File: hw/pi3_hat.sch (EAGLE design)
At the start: 117 parts, among them J1 XT30P, J2 XT30P, U1 AP64351SO8EP, U10 CAT24C32SOIC8, U11 STM32G474CEU6, U12 TCAN334GSOT23, U13 TCAN334GSOT23, U14 SPW2430HR5H-B, U2 DMMT5401, U3 DMG2305UX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

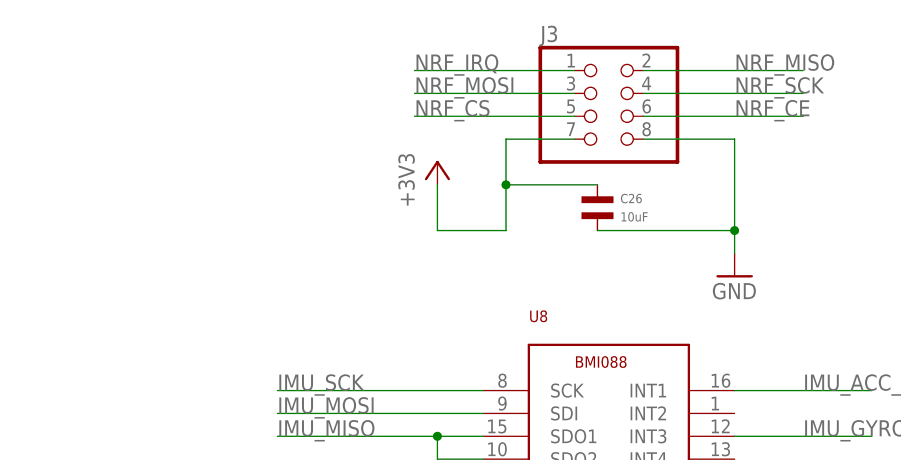
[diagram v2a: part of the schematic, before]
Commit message: Flip NRF around, add an LC filter and a ground plane
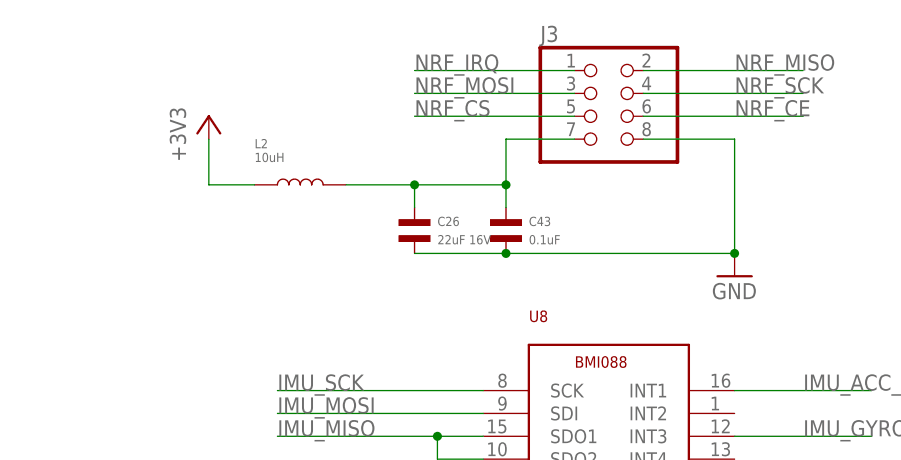
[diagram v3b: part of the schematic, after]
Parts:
- added C43: 0.1uF, mfpassives:CAPACITOR_NP_0402
- added L2: 10uH, mfpassives:INDUCTOR_1210
- C26: value 10uF -> 22uF 16V; device mfpassives:CAPACITOR_NP_1206 -> mfpassives:CAPACITOR_NP_1210; HOUSEPART YES -> (none); MF (none) -> SAMSUNG; MPN MF-CAP-1206-10uF -> CL32A226KOJNNNE
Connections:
- new net N$56: C26.P$1, C43.P$1, J3.7, L2.P$2
- net +3V3: now also L2.P$1; no longer C26.P$1, J3.7
- net GND: now also C43.P$2
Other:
- moved on the sheet: C26
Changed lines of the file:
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@@
 <part name="GND39" library="supply1" deviceset="GND" device=""/>
 <part name="+3V22" library="supply1" deviceset="+3V3" device=""/>
-<part name="C26" library="mfpassives" deviceset="CAPACITOR_NP" device="_1206" value="10uF">
-<attribute name="HOUSEPART" value="YES"/>
-<attribute name="MPN" value="MF-CAP-1206-10uF"/>
-</part>
 <part name="+3V25" library="supply1" deviceset="+3V3" device=""/>
 <part name="U10" library="pi3_hat" deviceset="CAT24C32" device="SOIC8">
@@
 <attribute name="MPN" value="MF-CAP-1206-10uF"/>
 </part>
+<part name="L2" library="mfpassives" deviceset="INDUCTOR" device="_1210" value="10uH">
+<attribute name="MPN" value="MF-IND-1210-10uH"/>
+</part>
+<part name="C43" library="mfpassives" deviceset="CAPACITOR_NP" device="_0402" value="0.1uF">
+<attribute name="HOUSEPART" value="YES"/>
+<attribute name="MPN" value="MF-CAP-0402-0.1uF"/>
+</part>
+<part name="C26" library="mfpassives" deviceset="CAPACITOR_NP" device="_1210" value="22uF 16V">
+<attribute name="MF" value="SAMSUNG"/>
+<attribute name="MPN" value="CL32A226KOJNNNE"/>
+</part>
 </parts>
 <sheets>
@@
 <attribute name="VALUE" x="812.8" y="307.34" size="1.778" layer="96"/>
 </instance>
-<instance part="+3V22" gate="G$1" x="782.32" y="322.58" smashed="yes">
-<attribute name="VALUE" x="779.78" y="317.5" size="1.778" layer="96" rot="R90"/>
-</instance>
-<instance part="C26" gate="G$1" x="800.1" y="317.5" smashed="yes">
-<attribute name="NAME" x="802.64" y="319.024" size="1.016" layer="95" font="vector" align="top-left"/>
-<attribute name="VALUE" x="802.64" y="315.976" size="1.016" layer="96" font="vector"/>
+<instance part="+3V22" gate="G$1" x="756.92" y="327.66" smashed="yes">
+<attribute name="VALUE" x="754.38" y="322.58" size="1.778" layer="96" rot="R90"/>
 </instance>
 <instance part="+3V25" gate="G$1" x="355.6" y="261.62" smashed="yes">
@@
 <attribute name="VALUE" x="801.624" y="60.96" size="1.016" layer="96" font="vector" rot="R90"/>
 </instance>
+<instance part="L2" gate="G$1" x="767.08" y="320.04" smashed="yes">
+<attribute name="NAME" x="762" y="325.12" size="1.016" layer="95" font="vector" align="top-left"/>
+<attribute name="VALUE" x="762" y="322.58" size="1.016" layer="96" font="vector"/>
+</instance>
+<instance part="C43" gate="G$1" x="789.94" y="314.96" smashed="yes">
+<attribute name="NAME" x="792.48" y="316.484" size="1.016" layer="95" font="vector" align="top-left"/>
+<attribute name="VALUE" x="792.48" y="313.436" size="1.016" layer="96" font="vector"/>
+</instance>
+<instance part="C26" gate="G$1" x="779.78" y="314.96" smashed="yes">
+<attribute name="MF" x="779.78" y="314.96" size="1.778" layer="96" display="off"/>
+<attribute name="NAME" x="782.32" y="316.484" size="1.016" layer="95" font="vector" align="top-left"/>
+<attribute name="VALUE" x="782.32" y="313.436" size="1.016" layer="96" font="vector"/>
+</instance>
 </instances>
 <busses>
@@
 <pinref part="GND39" gate="1" pin="GND"/>
 <wire x1="805.18" y1="325.12" x2="815.34" y2="325.12" width="0.1524" layer="91"/>
-<wire x1="815.34" y1="325.12" x2="815.34" y2="314.96" width="0.1524" layer="91"/>
+<wire x1="815.34" y1="325.12" x2="815.34" y2="312.42" width="0.1524" layer="91"/>
+<wire x1="789.94" y1="312.42" x2="815.34" y2="312.42" width="0.1524" layer="91"/>
+<junction x="815.34" y="312.42"/>
+<pinref part="C43" gate="G$1" pin="P$2"/>
 <pinref part="C26" gate="G$1" pin="P$2"/>
-<wire x1="815.34" y1="314.96" x2="815.34" y2="312.42" width="0.1524" layer="91"/>
-<wire x1="800.1" y1="314.96" x2="815.34" y2="314.96" width="0.1524" layer="91"/>
-<junction x="815.34" y="314.96"/>
+<wire x1="779.78" y1="312.42" x2="789.94" y2="312.42" width="0.1524" layer="91"/>
+<junction x="789.94" y="312.42"/>
 </segment>
 <segment>
@@
 </segment>
 <segment>
-<pinref part="+3V22" gate="G$1" pin="+3V3"/>
-<wire x1="782.32" y1="320.04" x2="782.32" y2="314.96" width="0.1524" layer="91"/>
-<wire x1="782.32" y1="314.96" x2="789.94" y2="314.96" width="0.1524" layer="91"/>
-<wire x1="789.94" y1="314.96" x2="789.94" y2="320.04" width="0.1524" layer="91"/>
-<pinref part="J3" gate="A" pin="7"/>
-<wire x1="789.94" y1="320.04" x2="789.94" y2="325.12" width="0.1524" layer="91"/>
-<wire x1="789.94" y1="325.12" x2="797.56" y2="325.12" width="0.1524" layer="91"/>
-<pinref part="C26" gate="G$1" pin="P$1"/>
-<wire x1="789.94" y1="320.04" x2="800.1" y2="320.04" width="0.1524" layer="91"/>
-<junction x="789.94" y="320.04"/>
-</segment>
-<segment>
 <pinref part="U4" gate="G$1" pin="VBAT"/>
 <pinref part="+3V25" gate="G$1" pin="+3V3"/>
@@
 <wire x1="802.64" y1="63.5" x2="792.48" y2="63.5" width="0.1524" layer="91"/>
 </segment>
+<segment>
+<pinref part="+3V22" gate="G$1" pin="+3V3"/>
+<wire x1="756.92" y1="325.12" x2="756.92" y2="320.04" width="0.1524" layer="91"/>
+<pinref part="L2" gate="G$1" pin="P$1"/>
+<wire x1="756.92" y1="320.04" x2="762" y2="320.04" width="0.1524" layer="91"/>
+</segment>
 </net>
 <net name="PI_TX_3V" class="0">
@@
 </segment>
 </net>
+<net name="N$56" class="0">
+<segment>
+<wire x1="772.16" y1="320.04" x2="779.78" y2="320.04" width="0.1524" layer="91"/>
+<pinref part="J3" gate="A" pin="7"/>
+<wire x1="779.78" y1="320.04" x2="789.94" y2="320.04" width="0.1524" layer="91"/>
+<wire x1="789.94" y1="320.04" x2="789.94" y2="325.12" width="0.1524" layer="91"/>
+<wire x1="789.94" y1="325.12" x2="797.56" y2="325.12" width="0.1524" layer="91"/>
+<wire x1="789.94" y1="320.04" x2="789.94" y2="317.5" width="0.1524" layer="91"/>
+<junction x="789.94" y="320.04"/>
+<pinref part="L2" gate="G$1" pin="P$2"/>
+<pinref part="C43" gate="G$1" pin="P$1"/>
+<pinref part="C26" gate="G$1" pin="P$1"/>
+<wire x1="779.78" y1="317.5" x2="779.78" y2="320.04" width="0.1524" layer="91"/>
+<junction x="779.78" y="320.04"/>
+</segment>
+</net>

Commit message: Update board rev to 4.1, since we haven't made one of those yet
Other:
- note added: "mjbots pi3 hat r4.1 (c) jjp@pobox.com 2020 Licensed under the Apache 2.0 License"
- note removed: "mjbots pi3 hat r4.2 (c) jjp@pobox.com 2020 Licensed under the Apache 2.0 License"
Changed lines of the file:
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@@
 <wire x1="-48.26" y1="170.18" x2="-48.26" y2="347.98" width="0.1524" layer="90"/>
 <text x="-45.72" y="335.28" size="7.62" layer="90" font="vector">INPUT POWER</text>
-<text x="-45.72" y="355.6" size="7.62" layer="90" font="vector">mjbots pi3 hat r4.2
+<text x="-45.72" y="355.6" size="7.62" layer="90" font="vector">mjbots pi3 hat r4.1
 (c) jjp@pobox.com 2020
 Licensed under the Apache 2.0 License</text>

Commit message: Add MPN for LTC2875
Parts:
- U9: MF (none) -> Analog; MPN (none) -> LTC2875IS8#PBF; POPULATE (none) -> 1
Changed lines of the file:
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@@
 <attribute name="POPULATE" value="0"/>
 </part>
-<part name="U9" library="pi3_hat" deviceset="LTC2875" device=""/>
+<part name="U9" library="pi3_hat" deviceset="LTC2875" device="">
+<attribute name="MF" value="Analog"/>
+<attribute name="MPN" value="LTC2875IS8#PBF"/>
+<attribute name="POPULATE" value="1"/>
+</part>
 <part name="JP2" library="pinhead" library_urn="urn:adsk.eagle:library:325" deviceset="PINHD-1X5" device="" package3d_urn="urn:adsk.eagle:package:22469/2">
 <attribute name="MF" value="MacroFab"/>
@@
 <attribute name="NAME" x="795.3756" y="235.1786" size="2.0828" layer="95" ratio="6" rot="SR0"/>
 <attribute name="VALUE" x="794.7406" y="232.6386" size="2.0828" layer="96" ratio="6" rot="SR0"/>
+<attribute name="MF" x="779.78" y="226.06" size="1.778" layer="96" display="off"/>
+<attribute name="MPN" x="779.78" y="226.06" size="1.778" layer="96" display="off"/>
+<attribute name="POPULATE" x="779.78" y="226.06" size="1.778" layer="96" display="off"/>
 </instance>
 <instance part="JP2" gate="A" x="655.32" y="228.6" smashed="yes" rot="R180">

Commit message: Switch capacitors and shift the NRF header a bit further up
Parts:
- C2, C3: MPN CGA5L1X7R1H106K160AC -> C3216X7R1H106K160AE
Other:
- note added: "mjbots pi3 hat r4.2 (c) jjp@pobox.com 2020 Licensed under the Apache 2.0 License"
- note removed: "mjbots pi3 hat r4.1 (c) jjp@pobox.com 2020 Licensed under the Apache 2.0 License"
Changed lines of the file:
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@@
 <drawing>
 <settings>
-<setting alwaysvectorfont="no"/>
+<setting alwaysvectorfont="yes"/>
 <setting keepoldvectorfont="yes"/>
 <setting verticaltext="up"/>
@@
 <part name="C2" library="mfpassives" deviceset="CAPACITOR_NP" device="_1206" value="10uF 50V">
 <attribute name="MF" value="TDK"/>
-<attribute name="MPN" value="CGA5L1X7R1H106K160AC"/>
+<attribute name="MPN" value="C3216X7R1H106K160AE"/>
 </part>
 <part name="C7" library="mfpassives" deviceset="CAPACITOR_NP" device="_1210" value="22uF 16V">
@@
 <part name="C3" library="mfpassives" deviceset="CAPACITOR_NP" device="_1206" value="10uF 50V">
 <attribute name="MF" value="TDK"/>
-<attribute name="MPN" value="CGA5L1X7R1H106K160AC"/>
+<attribute name="MPN" value="C3216X7R1H106K160AE"/>
 </part>
 <part name="GND11" library="supply1" deviceset="GND" device=""/>
@@
 <wire x1="-48.26" y1="170.18" x2="-48.26" y2="347.98" width="0.1524" layer="90"/>
 <text x="-45.72" y="335.28" size="7.62" layer="90" font="vector">INPUT POWER</text>
-<text x="-45.72" y="355.6" size="7.62" layer="90" font="vector">mjbots pi3 hat r4.1
+<text x="-45.72" y="355.6" size="7.62" layer="90" font="vector">mjbots pi3 hat r4.2
 (c) jjp@pobox.com 2020
 Licensed under the Apache 2.0 License</text>

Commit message: Draft of a r4.3 board
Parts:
- removed C41: 0.1uF, mfpassives:CAPACITOR_NP_0402
- removed C42: 10uF, mfpassives:CAPACITOR_NP_1206
- removed U14: SPW2430HR5H-B, SPW2430HR5H-B:SPW2430HR5H-B
- added JP6: (no value), pinhead:PINHD-1X3
- added R21: 105k, mfpassives:RESISTOR_0402
- C6: value 4.7nF -> 10uF; device mfpassives:CAPACITOR_NP_0402 -> mfpassives:CAPACITOR_NP_1206; MPN MF-CAP-0402-4.7nF -> MF-CAP-1206-10uF
- D8: value 36V -> 48V; MPN SMF36A-E3-08 -> SMF48A-E3-08
- L1: value 6.8uH 3.7A -> 10uF; device pi3_hat:INDUCTORTAIYO_8040 -> pi3_hat:NS10165T100MNA; HOUSEPART 0 -> (none); MF TAIYO YUDEN -> (none); MPN NR8040T6R8N -> NS10165T100MNA
- R1: value 15k -> 4.7k; MPN MF-RES-0402-15K -> MF-RES-0402-4.7K
- R2: value 115k -> 105k; MPN RC0402FR-07115KL -> RC0402FR-07105KL
- U1: value AP64351SO8EP -> MAX17504ATP+T; device pi3_hat:AP64351SO8EP -> pi3_hat:MAX17504ATP+T; MPN AP64351SP-13 -> MAX17504ATP+T; POPULATE (none) -> 1
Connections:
- net N$24 renamed FB
- removed net MIC_IN: C42.P$2, U7.PB10
- removed net N$22: R1.P$1, U1.COMP
- removed net N$59: C42.P$1, U14.OUTPUT
- new net V+SENSE: R1.P$1, R21.P$2, U7.PC4
- net +3V3: now also JP6.2; no longer C41.P$1, U14.VDD
- net +5V: now also JP6.1
- net 5VSW: now also L1.2, U1.LX, U1.LX_2, U1.LX_3; no longer L1.P$1, U1.SW
- net GND: now also JP6.3, R1.P$2, U1.EPAD, U1.PGND, U1.PGND_2, U1.PGND_3, U1.SGND; no longer C41.P$2, U1.GND, U14.GND
- net N$21: now also U1.VCC; no longer R1.P$2
- net REGOUT: now also L1.1; no longer L1.P$2
- net V+: now also R21.P$1
- net V+FUSED: now also U1.EN/UVLO, U1.VIN_2, U1.VIN_3; no longer U1.EN
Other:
- note added: "mjbots pi3 hat r4.3 (c) jjp@pobox.com 2020 Licensed under the Apache 2.0 License"
- note removed: "mjbots pi3 hat r4.2 (c) jjp@pobox.com 2020 Licensed under the Apache 2.0 License"
- moved on the sheet: C1, C2, C3, C4, C5, C6, C7, C8, D1, D8, F1, J1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

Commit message: Rev hw to r4.4  * Move C1 silk to not be on a pad  * Use a fuse rated for the new input voltage
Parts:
- F1: DPN MFU06034.00CT-ND -> 507-2154-1-ND; MF VISHAY -> BEL FUSE; MPN MFU0603FF04000P100 -> 0686F4000-01; VENDOR (none) -> BEL FUSE
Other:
- note added: "mjbots pi3 hat r4.4 (c) jjp@pobox.com 2020 Licensed under the Apache 2.0 License"
- note removed: "mjbots pi3 hat r4.3 (c) jjp@pobox.com 2020 Licensed under the Apache 2.0 License"
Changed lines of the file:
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@@
 <part name="P+4" library="supply1" deviceset="+5V" device=""/>
 <part name="F1" library="pi3_hat" deviceset="MFU0603FF04000P100" device="">
-<attribute name="DPN" value="MFU06034.00CT-ND"/>
+<attribute name="DPN" value="507-2154-1-ND"/>
 <attribute name="MANUFACTURER_PART_NUMBER" value=""/>
-<attribute name="MF" value="VISHAY"/>
-<attribute name="MPN" value="MFU0603FF04000P100"/>
-<attribute name="POPULATE" value="1"/>
+<attribute name="MF" value="BEL FUSE"/>
+<attribute name="MPN" value="0686F4000-01"/>
+<attribute name="POPULATE" value="1"/>
+<attribute name="VENDOR" value="BEL FUSE"/>
 </part>
 <part name="C2" library="mfpassives" deviceset="CAPACITOR_NP" device="_1206" value="10uF 50V">
@@
 <wire x1="-48.26" y1="170.18" x2="-48.26" y2="347.98" width="0.1524" layer="90"/>
 <text x="-45.72" y="335.28" size="7.62" layer="90" font="vector">INPUT POWER</text>
-<text x="-45.72" y="355.6" size="7.62" layer="90" font="vector">mjbots pi3 hat r4.3
+<text x="-45.72" y="355.6" size="7.62" layer="90" font="vector">mjbots pi3 hat r4.4
 (c) jjp@pobox.com 2020
 Licensed under the Apache 2.0 License</text>
